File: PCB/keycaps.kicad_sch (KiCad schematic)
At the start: 106 parts

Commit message: Add more keycaps
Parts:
- KC10, KC11, KC12, KC13, KC2, KC3, KC4, KC5: footprint clavier:KC_Cherry_MX_R1_1.00u_White -> clavier:KC_Cherry_MX_R1_1.00u_Black
- KC100, KC93, KC94, KC95, KC97, KC98, KC99: footprint (none) -> clavier:KC_Cherry_MX_R4_1.25u_Black
- KC101, KC102, KC103, KC89: footprint (none) -> clavier:KC_Cherry_MX_R4_1.00u_Black
- KC105, KC77, KC78, KC79, KC80, KC81, KC82, KC83, KC84, KC85, KC86, KC87, KC90, KC91, KC92: footprint (none) -> clavier:KC_Cherry_MX_R4_1.00u_White
- KC18, KC23, KC26, KC32, KC33, KC34, KC35, KC36, KC37, KC38: footprint (none) -> clavier:KC_Cherry_MX_R1_1.00u_Black
- KC19, KC20, KC21, KC22, KC24, KC25, KC27, KC28, KC29, KC30: footprint (none) -> clavier:KC_Cherry_MX_R1_1.00u_White
- KC31: footprint (none) -> clavier:KC_Cherry_MX_R1_2.00u_Black
- KC40, KC41, KC42, KC43, KC44, KC45, KC46, KC47, KC48, KC49, KC50, KC51, KC56, KC57, KC58: footprint (none) -> clavier:KC_Cherry_MX_R2_1.00u_White
- KC53, KC54, KC55: footprint (none) -> clavier:KC_Cherry_MX_R2_1.00u_Black
- KC60, KC61, KC62, KC64, KC65, KC67, KC68, KC69, KC70, KC71, KC72, KC73, KC74: footprint (none) -> clavier:KC_Cherry_MX_R3_1.00u_White
- KC63, KC66: footprint (none) -> clavier:KC_Cherry_MX_R3_1.00u_Barred_Black

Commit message: Add all missing keycaps
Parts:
- KC104: footprint (none) -> clavier:KC_Cherry_MX_R4_2.00u_White
- KC106: footprint (none) -> clavier:KC_Cherry_MX_R4-R4_1.00u_Black
- KC39: footprint (none) -> clavier:KC_Cherry_MX_R2_1.50u_Black
- KC52: footprint (none) -> clavier:KC_Cherry_MX_R2-R3_ISO_Enter_Black
- KC59: footprint (none) -> clavier:KC_Cherry_MX_R3_1.75u_Black
- KC75: footprint (none) -> clavier:KC_Cherry_MX_R2-R3_1.00u_Black
- KC76: footprint (none) -> clavier:KC_Cherry_MX_R4_1.25u_Black
- KC88: footprint (none) -> clavier:KC_Cherry_MX_R4_2.75u_Black
- KC96: footprint (none) -> clavier:KC_Cherry_MX_R4_6.25u_Black
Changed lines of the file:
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@@
 			)
 		)
-		(property "Footprint" ""
+		(property "Footprint" "clavier:KC_Cherry_MX_R4_1.25u_Black"
 			(at 44.45 184.15 0)
 			(effects
@@
 			)
 		)
-		(property "Footprint" ""
+		(property "Footprint" "clavier:KC_Cherry_MX_R4-R4_1.00u_Black"
 			(at 349.25 209.55 0)
 			(effects
@@
 			)
 		)
-		(property "Footprint" ""
+		(property "Footprint" "clavier:KC_Cherry_MX_R2-R3_ISO_Enter_Black"
 			(at 215.9 133.35 0)
 			(effects
@@
 			)
 		)
-		(property "Footprint" ""
+		(property "Footprint" "clavier:KC_Cherry_MX_R4_2.00u_White"
 			(at 317.5 209.55 0)
 			(effects
@@
 			)
 		)
-		(property "Footprint" ""
+		(property "Footprint" "clavier:KC_Cherry_MX_R3_1.75u_Black"
 			(at 44.45 158.75 0)
 			(effects
@@
 			)
 		)
-		(property "Footprint" ""
+		(property "Footprint" "clavier:KC_Cherry_MX_R4_2.75u_Black"
 			(at 203.2 184.15 0)
 			(effects
@@
 			)
 		)
-		(property "Footprint" ""
+		(property "Footprint" "clavier:KC_Cherry_MX_R4_6.25u_Black"
 			(at 114.3 209.55 0)
 			(effects
@@
 			)
 		)
-		(property "Footprint" ""
+		(property "Footprint" "clavier:KC_Cherry_MX_R2_1.50u_Black"
 			(at 44.45 133.35 0)
 			(effects
@@
 			)
 		)
-		(property "Footprint" ""
+		(property "Footprint" "clavier:KC_Cherry_MX_R2-R3_1.00u_Black"
 			(at 349.25 158.75 0)
 			(effects

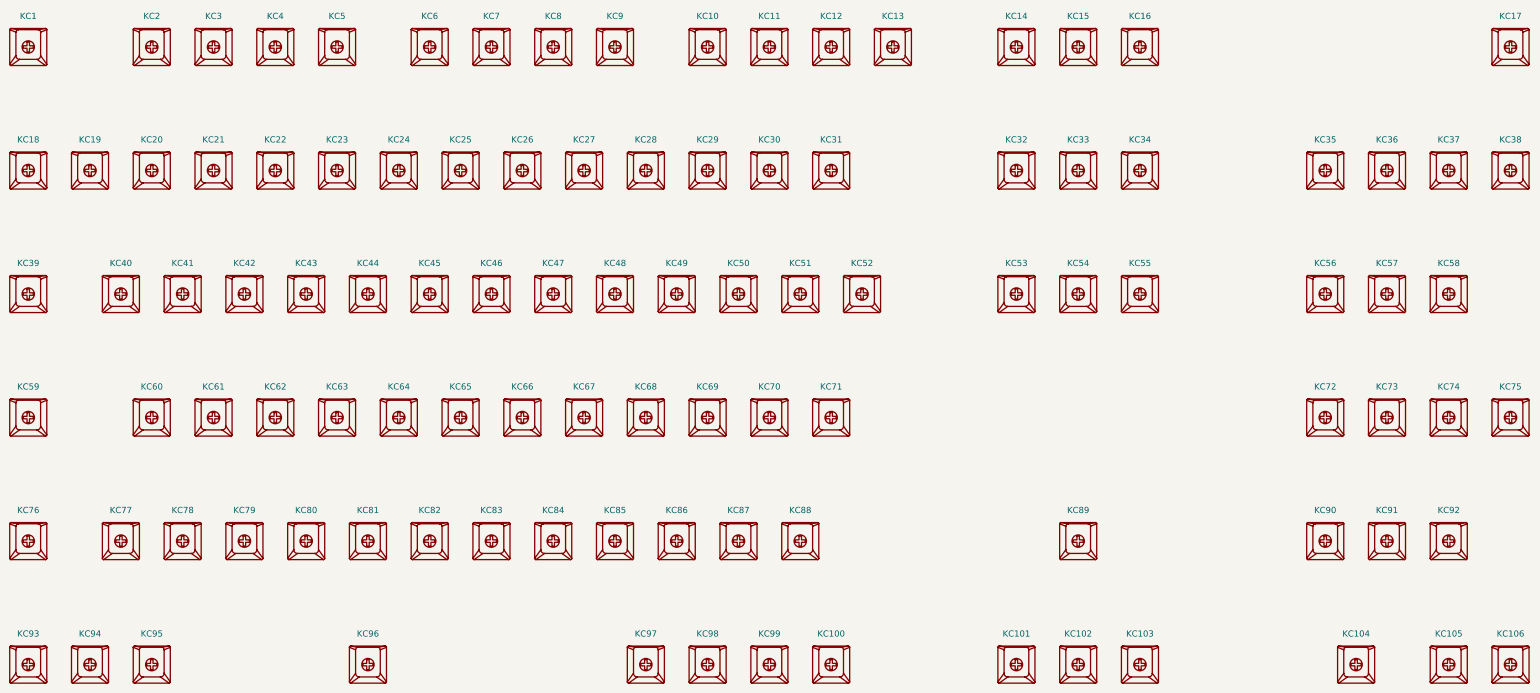
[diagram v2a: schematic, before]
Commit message: Add stabilizers
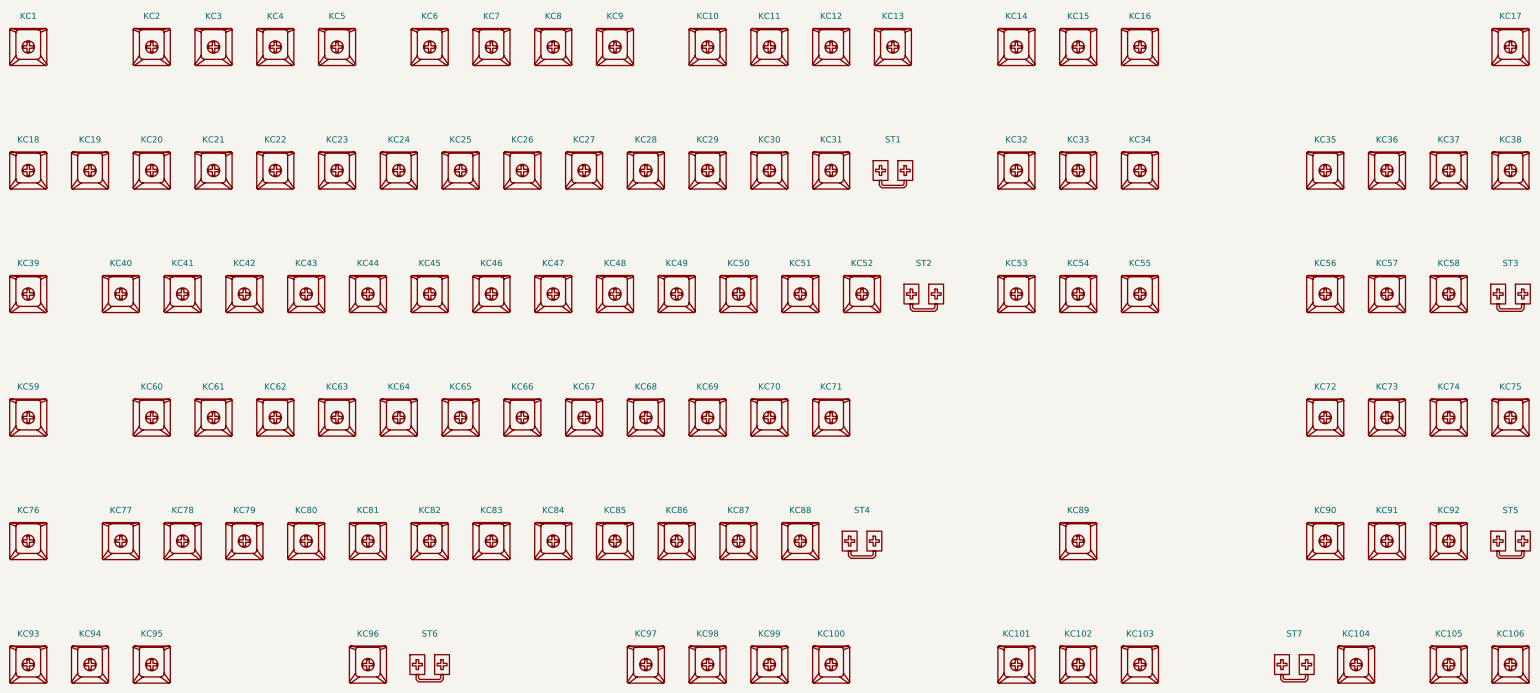
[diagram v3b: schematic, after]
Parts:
- added ST1, ST2, ST3, ST4, ST5, ST7: ~, clavier:Stabilizer_2.00u, symbol clavier:Stabilizer
- added ST6: ~, clavier:Stabilizer_6.25u, symbol clavier:Stabilizer

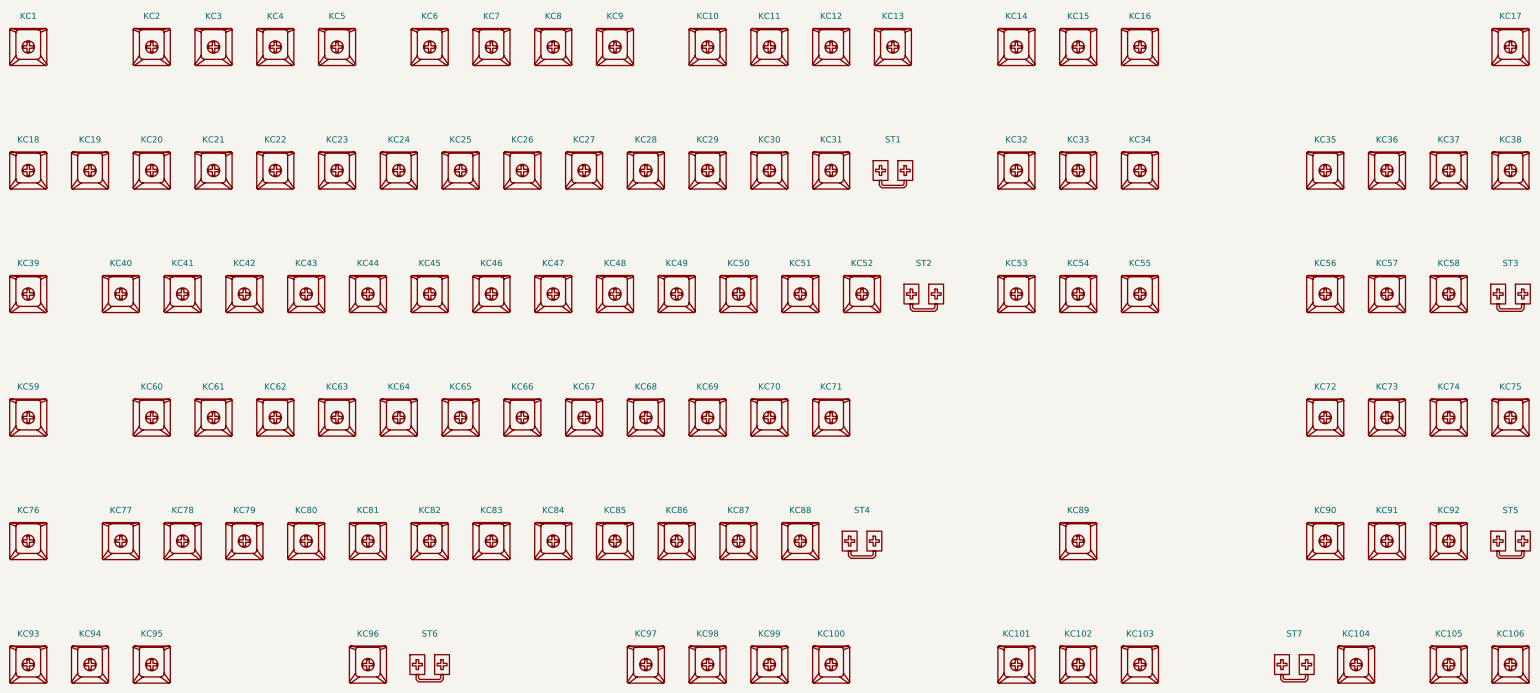
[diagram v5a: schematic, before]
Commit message: Complete the PCB routing
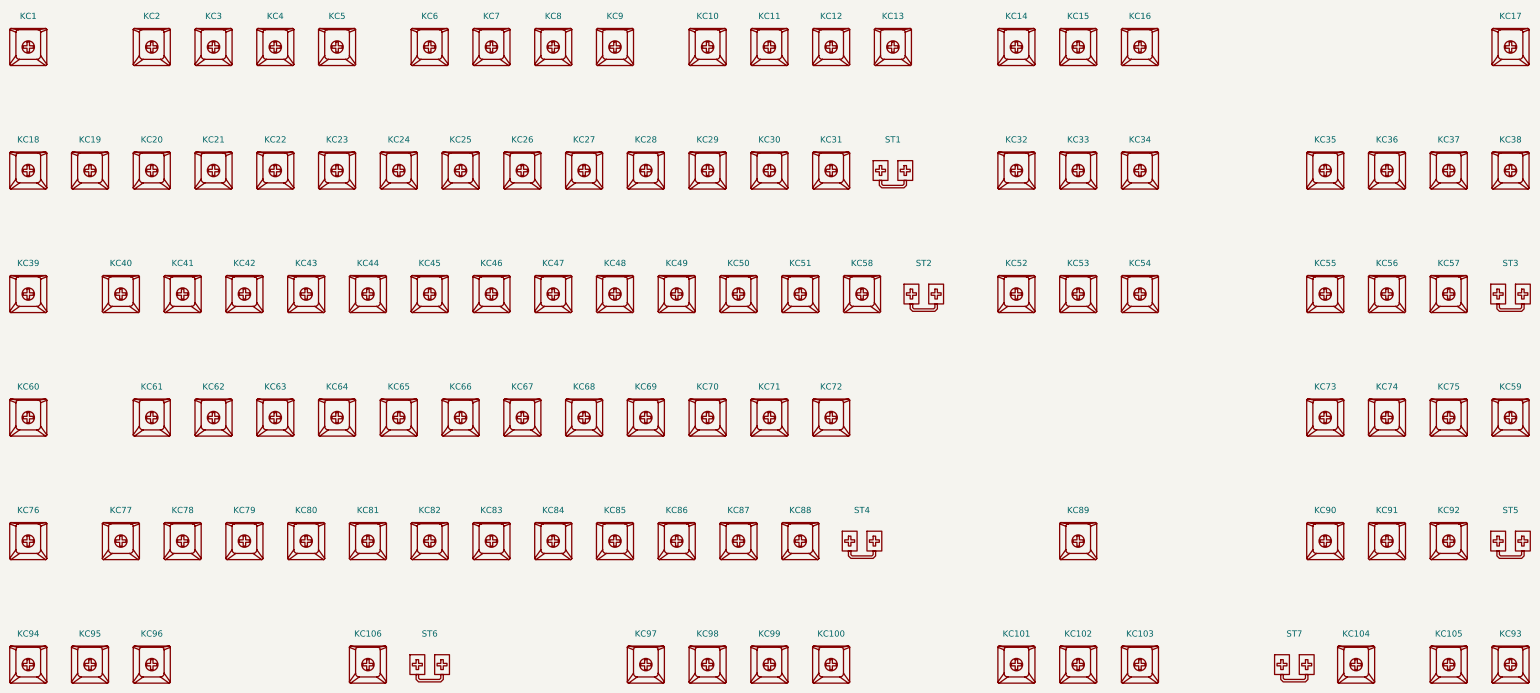
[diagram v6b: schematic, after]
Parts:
- renumbered KC96 to KC106, KC53 to KC52, KC54 to KC53, KC55 to KC54, KC56 to KC55, KC57 to KC56, KC58 to KC57, KC52 to KC58, KC75 to KC59, KC59 to KC60, KC60 to KC61, KC61 to KC62, KC62 to KC63, KC63 to KC64, KC64 to KC65, KC65 to KC66, KC66 to KC67, KC67 to KC68, KC68 to KC69, KC69 to KC70, KC70 to KC71, KC71 to KC72, KC72 to KC73, KC73 to KC74, KC74 to KC75, KC106 to KC93, KC93 to KC94, KC94 to KC95, KC95 to KC96
